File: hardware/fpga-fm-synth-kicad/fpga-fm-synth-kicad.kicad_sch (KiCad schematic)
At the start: 8 parts, among them J2 Conn_01x06_Socket, J3 DIN-5_180degree, U1 TangNano20K, U2 BlackPill_STLINK, U3 H11L1

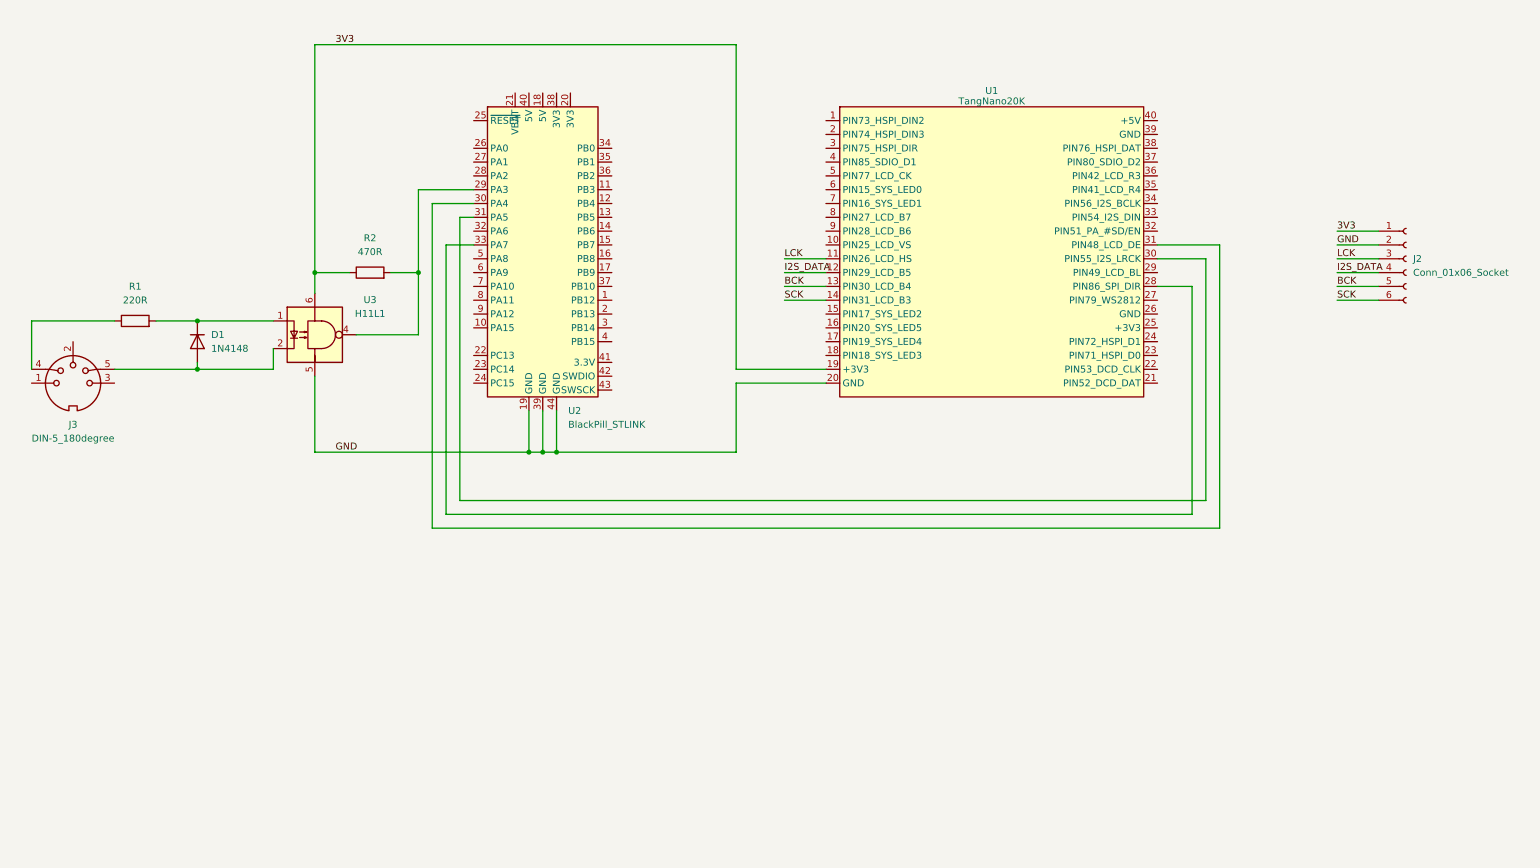
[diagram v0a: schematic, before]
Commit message: improved kicad schematic
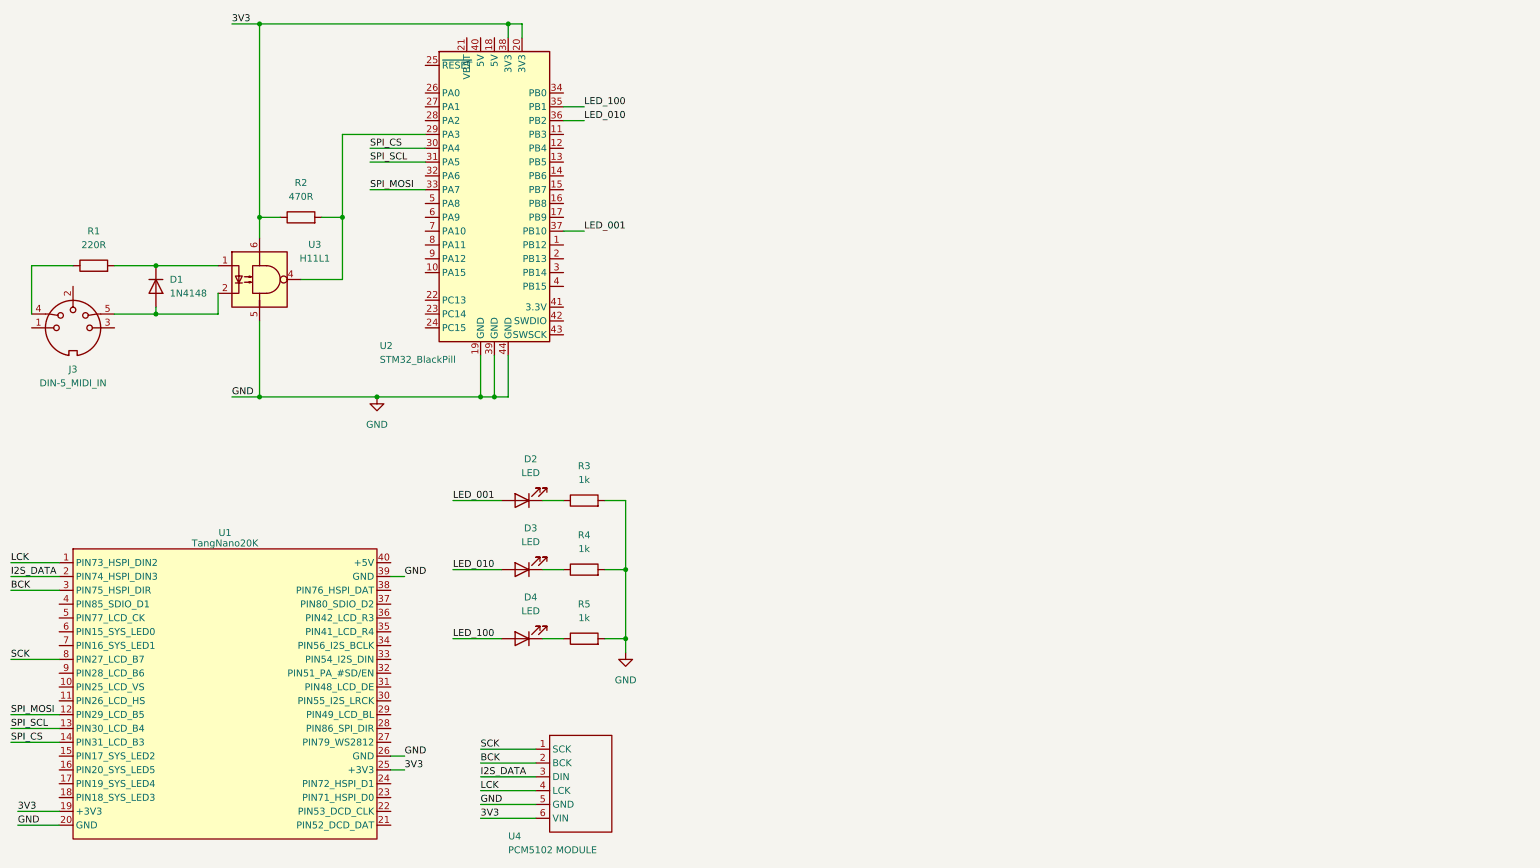
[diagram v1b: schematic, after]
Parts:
- removed J2: Conn_01x06_Socket, symbol Connector:Conn_01x06_Socket
- added D2, D3, D4: LED, symbol Device:LED
- added R3, R4, R5: 1k, symbol Device:R
- added U4: PCM5102 MODULE, symbol pcm5102module:PCM5102_module
- J3: value DIN-5_180degree -> DIN-5_MIDI_IN
- U2: value BlackPill_STLINK -> STM32_BlackPill
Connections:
- net 3V3: now also U1.25 (+3V3), U2.20 (3V3), U2.38 (3V3), U4.6 (VIN)
- net BCK: now also U1.3 (PIN75_HSPI_DIR), U4.2 (BCK); no longer U1.13 (PIN30_LCD_B4)
- net GND: now also U1.26 (GND), U1.39 (GND), R3.2, R4.2, R5.2, U4.5 (GND)
- net I2S_DATA: now also U1.2 (PIN74_HSPI_DIN3), U4.3 (DIN); no longer U1.12 (PIN29_LCD_B5)
- net LCK: now also U1.1 (PIN73_HSPI_DIN2), U4.4 (LCK); no longer U1.11 (PIN26_LCD_HS)
- net SCK: now also U1.8 (PIN27_LCD_B7), U4.1 (SCK); no longer U1.14 (PIN31_LCD_B3)
- net at U1.28 (PIN86_SPI_DIR): no longer U2.33 (PA7)
- net at U1.30 (PIN55_I2S_LRCK): no longer U2.31 (PA5)
- net at U1.31 (PIN48_LCD_DE): no longer U2.30 (PA4)
- net LED_100: now reaches U2.35 (PB1)
- net LED_100: now also D4.2 (A)
- net LED_010: now reaches U2.36 (PB2)
- net LED_010: now also D3.2 (A)
- net LED_001: now reaches U2.37 (PB10)
- net LED_001: now also D2.2 (A)
- new net: D3.1 (K), R4.1
- new net: D4.1 (K), R5.1
- new net: D2.1 (K), R3.1
- new net SPI_CS: U1.14 (PIN31_LCD_B3), U2.30 (PA4)
- new net SPI_MOSI: U1.12 (PIN29_LCD_B5), U2.33 (PA7)
- new net SPI_SCL: U1.13 (PIN30_LCD_B4), U2.31 (PA5)
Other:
- company: (none) -> Jakub Romankiewicz
- title: (none) -> FPGA FM Synthesizer
- moved on the sheet: D1, J3, R1, R2, U1, U2, U3
